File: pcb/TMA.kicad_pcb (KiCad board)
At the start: 2 copper layers, 18 x 18 mm, 22 parts, among them J1 Conn_01x02, J2 Conn_01x05, J3 Conn_01x04, J4 Conn_01x02, U1 BMP280, U2 BMI160, U3 ATtiny1614-SS, U4 MIC5504-3.3YM5

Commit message: Minor clean up.
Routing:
- net +3V3: track 55.1 -> 54.4 mm

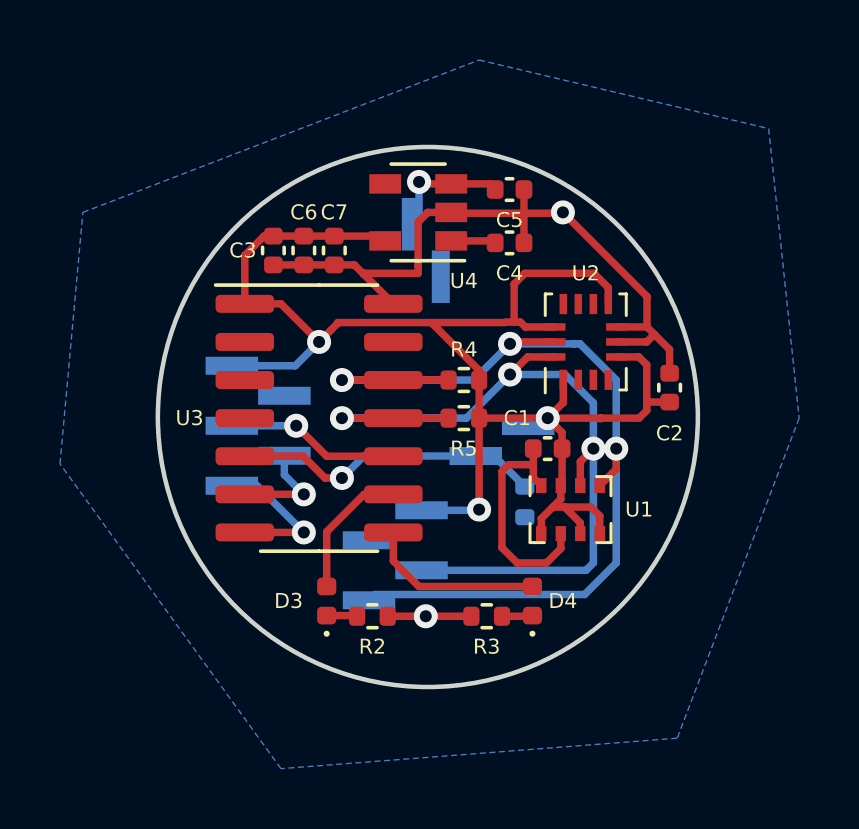
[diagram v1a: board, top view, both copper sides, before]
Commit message: fix lipo connection, move R1 to front
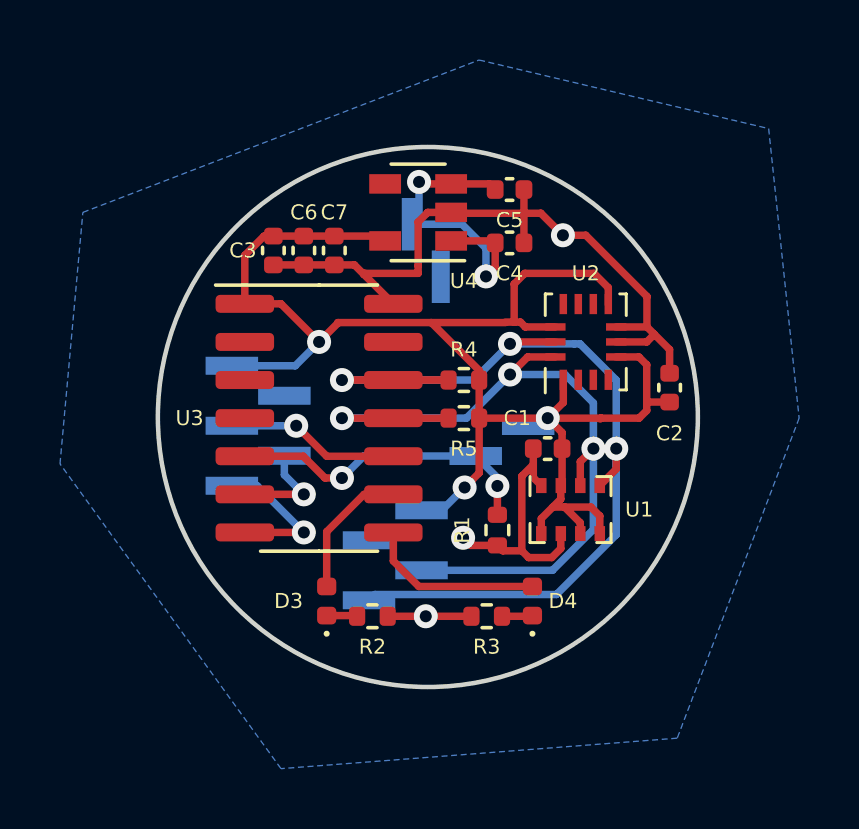
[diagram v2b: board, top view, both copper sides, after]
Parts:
- R1: moved to F.Cu
- moved R1 1.31 mm to (77.3, 53.8)
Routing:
- net Net-(C4-Pad1): track 5.66 -> 10.7 mm, vias 1 -> 2
- net MODE: track 10.4 -> 11.2 mm, vias 1 -> 2
- net +3V3: track 54.4 -> 53.7 mm
- net SDA: track 27.3 -> 26.6 mm
- net GND: track 34.8 -> 35.4 mm, vias 2 -> 3
- net SCL: track 31.5 -> 31.0 mm
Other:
- net class Default removed
